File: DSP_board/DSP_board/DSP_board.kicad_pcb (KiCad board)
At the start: 2 copper layers, 143.5 x 100.1 mm, 88 parts, among them IC5 F280025CPNQR, J1 Conn_01x02, J2 Conn_01x02, J3 Conn_01x02, J4 Conn_01x02, J5 1-84981-0, J6 Conn_01x02

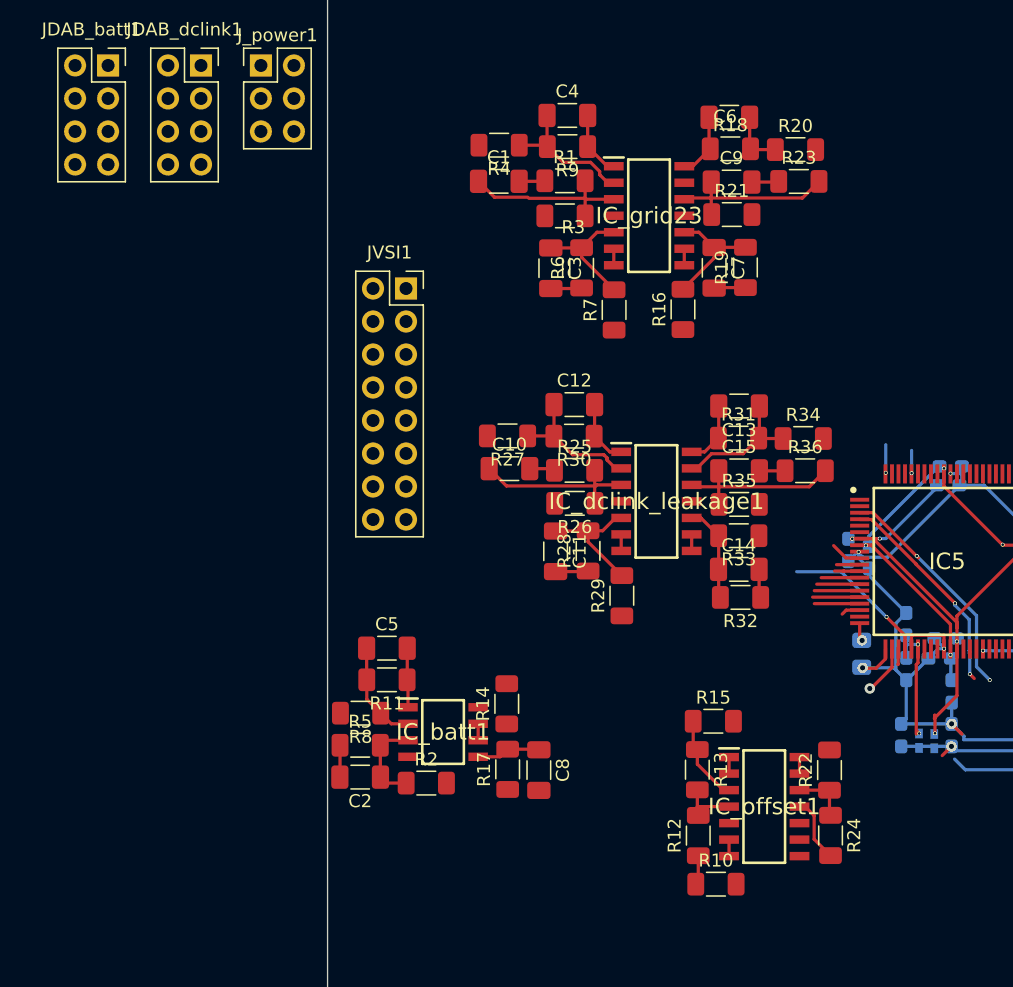
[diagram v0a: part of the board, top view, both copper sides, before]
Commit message: connected ADC's
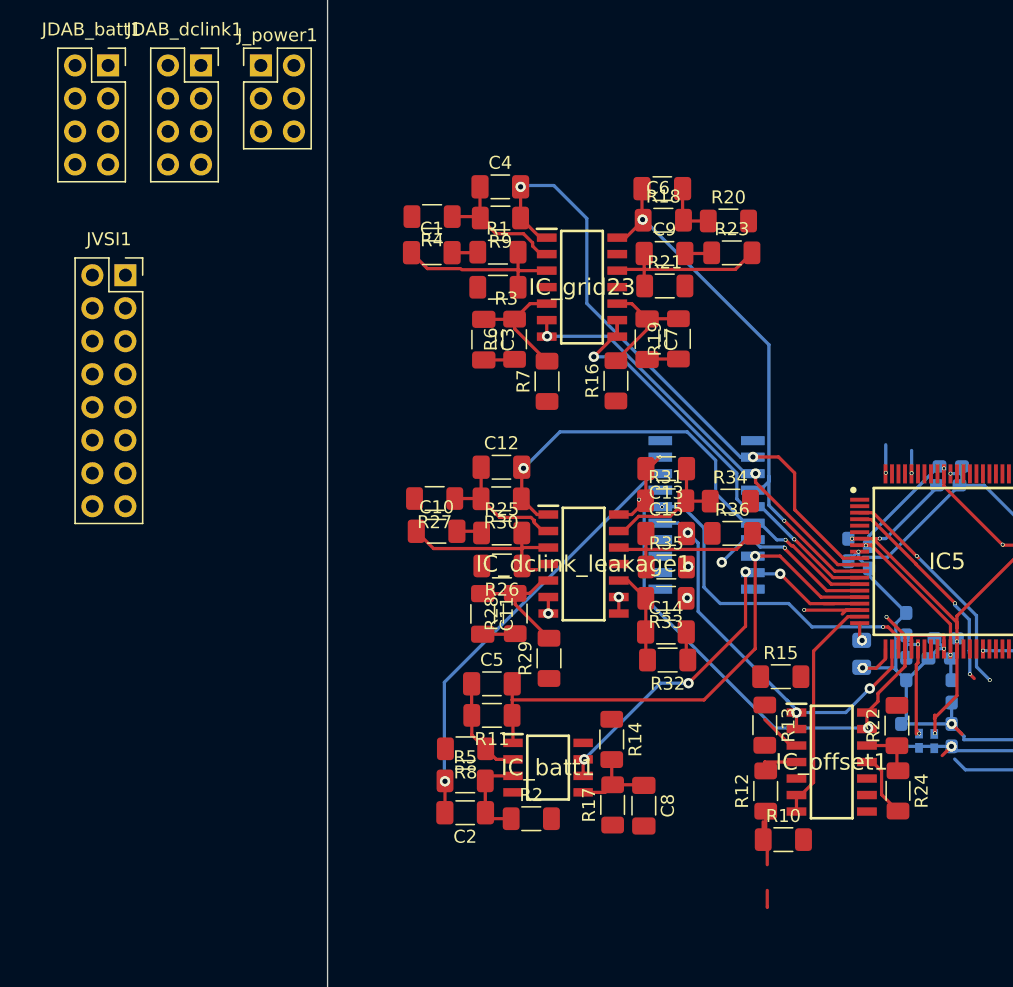
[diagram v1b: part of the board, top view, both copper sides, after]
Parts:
- added IC1: SN74S1053NSR, sn74s:sn74, B.Cu at (114.5, 85.8)
- moved JVSI1 21.6 mm to (69.7, 67.3)
- moved R14 8.53 mm to (107.2, 103.1), turned to -90 degrees
- moved C5 8.53 mm to (97.9, 98.8)
- moved R11 8.53 mm to (97.9, 101.2)
- moved R8 8.53 mm to (95.9, 103.8)
- moved C2 8.53 mm to (95.9, 108.7)
- moved IC_batt1 8.53 mm to (102.2, 105.2)
- moved C8 8.53 mm to (109.6, 108.2)
- moved R17 8.53 mm to (107.2, 108.1)
- moved R2 8.53 mm to (101.0, 109.2)
- moved R5 8.53 mm to (95.9, 106.2)
- moved R1 7.54 mm to (98.4, 65.6)
- moved R3 7.54 mm to (98.4, 68.3)
- moved IC_grid23 7.54 mm to (104.9, 68.2)
- moved R23 7.54 mm to (116.4, 65.6)
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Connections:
- B1 pad 14: offset_v -> voltage_offset
- B1 pad 18: offset_i -> curr_offset
- B1 pad 19: unconnected-(B1-Pad19) -> batt_curr_offset
- B1 pad 42: unconnected-(B1-Pad42) -> /controller_sheet/i2ca_scl
- B1 pad 43: unconnected-(B1-Pad43) -> /controller_sheet/i2ca_sda
- B1 pad 51: unconnected-(B1-Pad51) -> /controller_sheet/en_dab
- B1 pad 52: unconnected-(B1-Pad52) -> /controller_sheet/en_vsi
- C1 pad 2: /curr_offset -> curr_offset
- C10 pad 2: /curr_offset -> curr_offset
- C11 pad 2: /voltage_offset -> voltage_offset
- C15 pad 2: /curr_offset -> curr_offset
- C2 pad 2: /batt_curr_offset -> batt_curr_offset
- C3 pad 2: /voltage_offset -> voltage_offset
- C7 pad 2: /voltage_offset -> voltage_offset
- C9 pad 2: /curr_offset -> curr_offset
- IC5 pad 19: unconnected-(IC5-Pad19) -> batt_curr_offset
- IC5 pad 22: offset_i -> curr_offset
- IC5 pad 24: offset_v -> voltage_offset
- IC5 pad 39: unconnected-(IC5-Pad39) -> /controller_sheet/en_vsi
- IC5 pad 40: unconnected-(IC5-Pad40) -> /controller_sheet/en_dab
- IC5 pad 43: unconnected-(IC5-Pad43) -> /controller_sheet/i2ca_sda
- IC5 pad 44: unconnected-(IC5-Pad44) -> /controller_sheet/i2ca_scl
- IC_offset1 pad 1: Net-(IC_offset1-Pad1) -> curr_offset
- IC_offset1 pad 13: /voltage_offset -> voltage_offset
- IC_offset1 pad 14: /voltage_offset -> voltage_offset
- IC_offset1 pad 2: Net-(IC_offset1-Pad1) -> curr_offset
- IC_offset1 pad 6: /batt_curr_offset -> batt_curr_offset
- IC_offset1 pad 7: /batt_curr_offset -> batt_curr_offset
- R1 pad 1: /curr_offset -> curr_offset
- R19 pad 1: /voltage_offset -> voltage_offset
- R23 pad 1: /curr_offset -> curr_offset
- R25 pad 1: /curr_offset -> curr_offset
- R28 pad 1: /voltage_offset -> voltage_offset
- R36 pad 1: /curr_offset -> curr_offset
- R5 pad 1: /batt_curr_offset -> batt_curr_offset
- R6 pad 1: /voltage_offset -> voltage_offset
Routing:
- net offset_i: track 113.0 -> 0.00 mm, vias 1 -> 0
- net (no net): track 0.00 -> 109.2 mm
- net batt_curr_offset: track 0.00 -> 51.0 mm, vias 0 -> 1
- net voltage_offset: track 0.00 -> 48.4 mm, vias 0 -> 2
- net Igrid3_sense: track 7.21 -> 48.5 mm, vias 0 -> 2
- net curr_offset: track 0.00 -> 37.5 mm, vias 0 -> 3
- net Igrid2_sense: track 6.95 -> 41.9 mm, vias 0 -> 2
- net batt_curr_sense: track 8.20 -> 41.4 mm, vias 0 -> 1
- net Vdc_link: track 2.54 -> 35.6 mm, vias 0 -> 3
- net Igrid1_sense: track 8.33 -> 38.5 mm, vias 0 -> 2
- net Vgrid3_sense: track 3.05 -> 32.8 mm, vias 0 -> 2
- net Vgrid2_sense: track 4.23 -> 33.5 mm, vias 0 -> 2
- net batt_V_sense: track 76.3 -> 103.8 mm, vias 0 -> 4
- net Vgrid1_sense: track 4.76 -> 29.5 mm, vias 0 -> 3
- net I_leackage: track 67.4 -> 91.4 mm, vias 0 -> 3
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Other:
- copper layers 2 -> 4

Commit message: controller_final
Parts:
- removed C12, C13, C5, C6, C8: CAP, Capacitor_SMD:C_1206_3216Metric_Pad1.33x1.80mm_HandSolder
- removed IC_batt1: LM358S-13, LM324:SOIC127P600X175-8N
- removed JDAB_batt1, JDAB_dclink1: Conn_02x04_Odd_Even, Connector_PinSocket_2.54mm:PinSocket_2x04_P2.54mm_Vertical
- removed JVSI1: Conn_02x08_Odd_Even, Connector_PinSocket_2.54mm:PinSocket_2x08_P2.54mm_Vertical
- added J7: Conn_02x10_Odd_Even, Connector_PinSocket_2.54mm:PinSocket_2x10_P2.54mm_Vertical, F.Cu at (110.7, 72.0)
- added J8: Conn_02x06_Odd_Even, Connector_PinSocket_2.54mm:PinSocket_2x07_P2.54mm_Vertical, F.Cu at (117.0, 117.5)
- added J9: Conn_02x06_Odd_Even, Connector_PinSocket_2.54mm:PinSocket_2x06_P2.54mm_Vertical, F.Cu at (101.8, 108.4)
- added R42: R, Resistor_SMD:R_1206_3216Metric_Pad1.30x1.75mm_HandSolder, F.Cu at (164.9, 64.5)
- added R43: R, Resistor_SMD:R_1206_3216Metric_Pad1.30x1.75mm_HandSolder, F.Cu at (164.8, 67.0)
- added R44: R, Resistor_SMD:R_1206_3216Metric_Pad1.30x1.75mm_HandSolder, F.Cu at (164.8, 69.6)
- added R45: R, Resistor_SMD:R_1206_3216Metric_Pad1.30x1.75mm_HandSolder, F.Cu at (164.8, 130.1)
- added R46: R, Resistor_SMD:R_1206_3216Metric_Pad1.30x1.75mm_HandSolder, F.Cu at (164.8, 132.6)
- added R47: R, Resistor_SMD:R_1206_3216Metric_Pad1.30x1.75mm_HandSolder, F.Cu at (164.8, 135.1)
- added R48: R, Resistor_SMD:R_1206_3216Metric_Pad1.30x1.75mm_HandSolder, F.Cu at (164.8, 137.7)
- added R49: R, Resistor_SMD:R_1206_3216Metric_Pad1.30x1.75mm_HandSolder, F.Cu at (174.6, 130.2)
- added R50: R, Resistor_SMD:R_1206_3216Metric_Pad1.30x1.75mm_HandSolder, F.Cu at (174.6, 132.8)
- added R51: R, Resistor_SMD:R_1206_3216Metric_Pad1.30x1.75mm_HandSolder, F.Cu at (174.6, 135.4)
- added R52: R, Resistor_SMD:R_1206_3216Metric_Pad1.30x1.75mm_HandSolder, F.Cu at (174.6, 137.9)
- C1, C10, C11, C14, C15, C2, C3, C4, C7, C9, J5, R1, R13, R15, R16, R19, R2, R21, R23, R25, R26, R28, R29, R3, R32, R33, R35, R36, R4, R5, R6, R7, R8: moved to B.Cu
- IC1: moved to F.Cu
- moved R11 101.4 mm to (185.6, 50.3), turned to 0 degrees
- moved R27 93.4 mm to (186.0, 71.8), turned to 0 degrees
- moved R17 93.0 mm to (185.4, 57.9), turned to 0 degrees
- moved R14 91.6 mm to (185.4, 55.5), turned to 0 degrees
- moved R9 89.2 mm to (182.8, 92.3), turned to 0 degrees
- moved R12 85.9 mm to (185.7, 52.8), turned to 0 degrees
- moved R30 78.5 mm to (174.5, 64.4), turned to 0 degrees
- moved R18 74.4 mm to (185.5, 60.4)
- moved J_power1 71.6 mm to (150.0, 66.7), turned to 90 degrees
- moved R20 69.3 mm to (185.5, 62.8)
- moved R24 68.7 mm to (186.0, 68.4), turned to 0 degrees
- moved R22 67.3 mm to (185.9, 66.0), turned to 0 degrees
- moved R31 65.7 mm to (174.6, 67.0)
- moved R10 64.5 mm to (182.8, 94.7)
- moved R34 60.3 mm to (174.6, 69.7)
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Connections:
- B1 pad 103: VSI12 -> VSI21
- B1 pad 104: VSI21 -> VSI31
- B1 pad 105: VSI22 -> unconnected-(B1-Pad105)
- B1 pad 14: voltage_offset -> unconnected-(B1-Pad14)
- B1 pad 15: batt_curr_sense -> unconnected-(B1-Pad15)
- B1 pad 16: batt_V_sense -> unconnected-(B1-Pad16)
- B1 pad 17: I_leackage -> unconnected-(B1-Pad17)
- B1 pad 18: curr_offset -> unconnected-(B1-Pad18)
- B1 pad 19: batt_curr_offset -> unconnected-(B1-Pad19)
- B1 pad 20: Vgrid1_sense -> unconnected-(B1-Pad20)
- B1 pad 21: Igrid1_sense -> unconnected-(B1-Pad21)
- B1 pad 22: Vgrid2_sense -> unconnected-(B1-Pad22)
- B1 pad 23: Igrid2_sense -> unconnected-(B1-Pad23)
- B1 pad 24: Vgrid3_sense -> unconnected-(B1-Pad24)
- B1 pad 25: Igrid3_sense -> unconnected-(B1-Pad25)
- B1 pad 4: unconnected-(B1-Pad4) -> FPGA_3v3
- B1 pad 42: /controller_sheet/i2ca_scl -> SCL
- B1 pad 43: /controller_sheet/i2ca_sda -> SDA
- B1 pad 54: /controller_sheet/pwm_dabb1 -> /controller_sheet/pwm_daba2
- B1 pad 55: /controller_sheet/pwm_daba2 -> /controller_sheet/pwmVSI3
- B1 pad 56: /controller_sheet/pwm_daba1 -> /controller_sheet/pwmVSI2
- B1 pad 57: /controller_sheet/pwmVSI3 -> /controller_sheet/pwmVSI1
- B1 pad 58: /controller_sheet/pwmVSI2 -> /controller_sheet/pwm_dabb1
- B1 pad 59: /controller_sheet/pwmVSI1 -> /controller_sheet/pwm_daba1
- B1 pad 60: unconnected-(B1-Pad60) -> DAB1PWM22
- B1 pad 61: unconnected-(B1-Pad61) -> DAB1PWM21
- B1 pad 62: unconnected-(B1-Pad62) -> DAB1PWM12
- B1 pad 63: unconnected-(B1-Pad63) -> DAB1PWM11
- B1 pad 66: DAB1PWM22 -> DAB2_PWM22
- B1 pad 67: DAB1PWM21 -> DAB2_PWM21
- B1 pad 68: DAB1PWM12 -> DAB2_PWM12
- B1 pad 69: DAB1PWM11 -> DAB2_PWM11
- B1 pad 78: DAB2_PWM22 -> unconnected-(B1-Pad78)
- B1 pad 79: DAB2_PWM21 -> unconnected-(B1-Pad79)
- B1 pad 80: DAB2_PWM12 -> unconnected-(B1-Pad80)
- B1 pad 81: DAB2_PWM11 -> unconnected-(B1-Pad81)
- B1 pad 84: unconnected-(B1-Pad84) -> OCD_grid1
- B1 pad 90: unconnected-(B1-Pad90) -> OCD_grd2
- B1 pad 91: unconnected-(B1-Pad91) -> OCD_grid3
- B1 pad 92: unconnected-(B1-Pad92) -> vsi_fault
- B1 pad 93: unconnected-(B1-Pad93) -> vsi_ready
- B1 pad 96: unconnected-(B1-Pad96) -> VSI12
- B1 pad 97: unconnected-(B1-Pad97) -> VSI22
- B1 pad 98: VSI31 -> VSI32
- B1 pad 99: VSI32 -> unconnected-(B1-Pad99)
- C1 pad 2: curr_offset -> offset_v
- C10 pad 2: curr_offset -> offset_v
- C11 pad 2: voltage_offset -> offset_v
- C15 pad 2: curr_offset -> offset_v
- C2 pad 2: batt_curr_offset -> offset_v
- C3 pad 2: voltage_offset -> offset_v
- C4 pad 2: Igrid3_sense -> ctrl_gnd
- C7 pad 2: voltage_offset -> offset_v
- C9 pad 2: curr_offset -> offset_v
- IC1 pad 12: Igrid3_sense -> Igrid2_sense
- IC1 pad 13: Vgrid3_sense -> Igrid3_sense
- IC1 pad 14: Igrid2_sense -> Vgrid3_sense
- IC1 pad 17: Vgrid1_sense -> I_leackage
- IC1 pad 18: batt_curr_sense -> Vgrid1_sense
- IC1 pad 19: batt_V_sense -> unconnected-(IC1-Pad19)
- IC1 pad 2: unconnected-(IC1-Pad2) -> batt_V_sense
- IC1 pad 3: unconnected-(IC1-Pad3) -> batt_curr_sense
- IC1 pad 4: unconnected-(IC1-Pad4) -> Vdc_link
- IC1 pad 5: curr_offset -> unconnected-(IC1-Pad5)
- IC1 pad 6: Vdc_link -> unconnected-(IC1-Pad6)
- IC1 pad 7: voltage_offset -> unconnected-(IC1-Pad7)
- IC1 pad 8: batt_curr_offset -> offset_v
- IC1 pad 9: I_leackage -> unconnected-(IC1-Pad9)
- IC5 pad 10: Igrid3_sense -> Igrid2_sense
- IC5 pad 11: Vgrid3_sense -> Igrid3_sense
- IC5 pad 12: Igrid2_sense -> Vgrid3_sense
- IC5 pad 15: Vgrid1_sense -> I_leackage
- IC5 pad 16: batt_curr_sense -> Vgrid1_sense
- IC5 pad 17: batt_V_sense -> Vdc_link
- IC5 pad 18: I_leackage -> batt_curr_sense
- IC5 pad 19: batt_curr_offset -> batt_V_sense
- IC5 pad 22: curr_offset -> offset_v
- IC5 pad 23: Vdc_link -> unconnected-(IC5-Pad23)
- IC5 pad 24: voltage_offset -> unconnected-(IC5-Pad24)
- IC5 pad 35: unconnected-(IC5-Pad35) -> dc_ready
- IC5 pad 37: unconnected-(IC5-Pad37) -> dc_fault
- IC5 pad 38: unconnected-(IC5-Pad38) -> OCD_leakage
- IC5 pad 39: /controller_sheet/en_vsi -> batt_fault
- IC5 pad 40: /controller_sheet/en_dab -> batt_ready
- IC5 pad 43: /controller_sheet/i2ca_sda -> SDA
- IC5 pad 44: /controller_sheet/i2ca_scl -> SCL
- IC5 pad 56: unconnected-(IC5-Pad56) -> /controller_sheet/en_dab
- IC5 pad 57: unconnected-(IC5-Pad57) -> /controller_sheet/en_vsi
- IC5 pad 74: unconnected-(IC5-Pad74) -> vsi_ready
- IC5 pad 75: unconnected-(IC5-Pad75) -> vsi_fault
- IC5 pad 77: unconnected-(IC5-Pad77) -> OCD_grid3
- IC5 pad 78: unconnected-(IC5-Pad78) -> OCD_grd2
- IC5 pad 79: unconnected-(IC5-Pad79) -> OCD_grid1
- IC_dclink_leakage1 pad 11: ctrl_gnd -> ctrl_-15
- IC_dclink_leakage1 pad 13: Net-(C13-Pad1) -> I_leackage
- IC_dclink_leakage1 pad 2: Net-(C12-Pad1) -> Igrid1_sense
- IC_grid23 pad 11: ctrl_gnd -> ctrl_-15
- IC_grid23 pad 13: Net-(C6-Pad1) -> Igrid2_sense
- IC_grid23 pad 2: Net-(C4-Pad1) -> Igrid3_sense
- IC_offset1 pad 1: curr_offset -> offset_v
- IC_offset1 pad 10: unconnected-(IC_offset1-Pad10) -> Net-(C4-Pad1)
- IC_offset1 pad 11: ctrl_gnd -> ctrl_-15
- IC_offset1 pad 12: Net-(IC_offset1-Pad12) -> unconnected-(IC_offset1-Pad12)
- IC_offset1 pad 13: voltage_offset -> unconnected-(IC_offset1-Pad13)
- IC_offset1 pad 14: voltage_offset -> unconnected-(IC_offset1-Pad14)
- IC_offset1 pad 2: curr_offset -> offset_v
- IC_offset1 pad 5: Net-(IC_offset1-Pad5) -> Net-(C2-Pad1)
- IC_offset1 pad 6: batt_curr_offset -> batt_curr_sense
- IC_offset1 pad 7: batt_curr_offset -> batt_curr_sense
- IC_offset1 pad 8: unconnected-(IC_offset1-Pad8) -> batt_V_sense
- IC_offset1 pad 9: unconnected-(IC_offset1-Pad9) -> batt_V_sense
- R1 pad 1: curr_offset -> offset_v
- R10 pad 1: Net-(IC_offset1-Pad5) -> SCL
- R10 pad 2: ctrl_gnd -> FPGA_3v3
- R11 pad 1: batt_curr_sense -> /controller_sheet/pwm_daba1
- R11 pad 2: Net-(C5-Pad1) -> ctrl_gnd
- R12 pad 1: Net-(IC_offset1-Pad5) -> /controller_sheet/pwm_dabb1
- R12 pad 2: ctrl_15 -> ctrl_gnd
- R14 pad 1: batt_v -> /controller_sheet/pwmVSI1
- R14 pad 2: Net-(C8-Pad1) -> ctrl_gnd
- R17 pad 1: ctrl_gnd -> /controller_sheet/pwmVSI2
- R17 pad 2: Net-(C8-Pad1) -> ctrl_gnd
- R18 pad 1: Igrid2_sense -> /controller_sheet/pwmVSI3
- R18 pad 2: Net-(C6-Pad1) -> ctrl_gnd
- R19 pad 1: voltage_offset -> offset_v
- R20 pad 1: Net-(C6-Pad1) -> /controller_sheet/pwm_daba2
- R20 pad 2: Igrid2_ref -> ctrl_gnd
- R22 pad 1: Net-(IC_offset1-Pad12) -> /controller_sheet/pwm_dabb2
- R22 pad 2: ctrl_15 -> ctrl_gnd
- R23 pad 1: curr_offset -> offset_v
- R24 pad 1: Net-(IC_offset1-Pad12) -> /controller_sheet/en_vsi
- R25 pad 1: curr_offset -> offset_v
- R27 pad 1: Net-(C12-Pad1) -> /controller_sheet/en_dab
- R27 pad 2: Igrid1_ref -> ctrl_gnd
- R28 pad 1: voltage_offset -> offset_v
- R30 pad 1: Igrid1_sense -> VSI32
- R30 pad 2: Net-(C12-Pad1) -> ctrl_gnd
- R31 pad 1: I_leackage -> VSI22
- R31 pad 2: Net-(C13-Pad1) -> ctrl_gnd
- R34 pad 1: Net-(C13-Pad1) -> VSI12
- R34 pad 2: curr_leakeage_ref -> ctrl_gnd
- R36 pad 1: curr_offset -> offset_v
- R4 pad 1: Net-(C4-Pad1) -> offset_v
- R4 pad 2: Igrid3_ref -> Net-(C2-Pad1)
- R5 pad 1: batt_curr_offset -> batt_v
- R5 pad 2: Net-(C2-Pad1) -> Net-(C4-Pad1)
- R6 pad 1: voltage_offset -> offset_v
- R8 pad 1: Net-(C5-Pad1) -> ctrl_gnd
- R8 pad 2: batt_curr_1 -> Net-(C4-Pad1)
- R9 pad 1: Igrid3_sense -> SDA
- R9 pad 2: Net-(C4-Pad1) -> FPGA_3v3
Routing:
- net ctrl_gnd: track 178.2 -> 609.5 mm, vias 7 -> 12
- net ctrl_-15: track 0.00 -> 136.1 mm, vias 0 -> 6
- net SDA: track 0.00 -> 122.8 mm, vias 0 -> 1
- net SCL: track 0.00 -> 119.8 mm, vias 0 -> 1
- net (no net): track 109.2 -> 0.00 mm
- net ctrl_15: track 85.6 -> 192.3 mm, vias 0 -> 5
- net ctrl_3v3: track 36.0 -> 126.8 mm, vias 2 -> 5
- net DAB1PWM22: track 0.00 -> 87.3 mm
- net DAB1PWM21: track 0.00 -> 86.7 mm
- net batt_V_sense: track 103.8 -> 17.9 mm, vias 4 -> 0
- net OCD_grid1: track 0.00 -> 85.9 mm
- net DAB1PWM11: track 0.00 -> 79.5 mm
- net DAB1PWM12: track 0.00 -> 78.5 mm
- net offset_v: track 0.00 -> 77.6 mm, vias 0 -> 5
- net /controller_sheet/pwm_daba1: track 2.16 -> 77.9 mm
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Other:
- board size 143.5 x 100.1 mm -> 134.2 x 94.8 mm
